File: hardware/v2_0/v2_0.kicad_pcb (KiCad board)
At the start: 4 copper layers, 106 parts, among them J1 USB_B_Mini, J10 SERV1, J11 SERV2, J12 SPI, J13 UART5, J14 NRFGPIO, J15 USB_B_Mini, J16 DRV1_MTR2, J17 DAC, J18 USB_A, J19 MTR1_CON, J2 CAN, J3 PWR, J4 Power_terminal, J5 DRV1_MTR1, J6 DRV1_MTR2, J7 MTR2_CON, J8 DRV1_MTR1, J9 USART3_UART4, P1 SWD, P2 NRFSWD, Q1 Q_NMOS_GSD, Q2 Q_NMOS_GSD, SW1 MCU_USB_POWER, SW2 NRF_USB_POWER, SW3 BOOT0, U1 TJA1051TK-3, U10 DRV8848, U2 STM32F40X_LQFP64, U3 BMI160, U4 MCP16311/2, U5 DRV8848, U8 BMD-340-A-R, U9 ADP2303ARDZ-5.0, Y1 8M

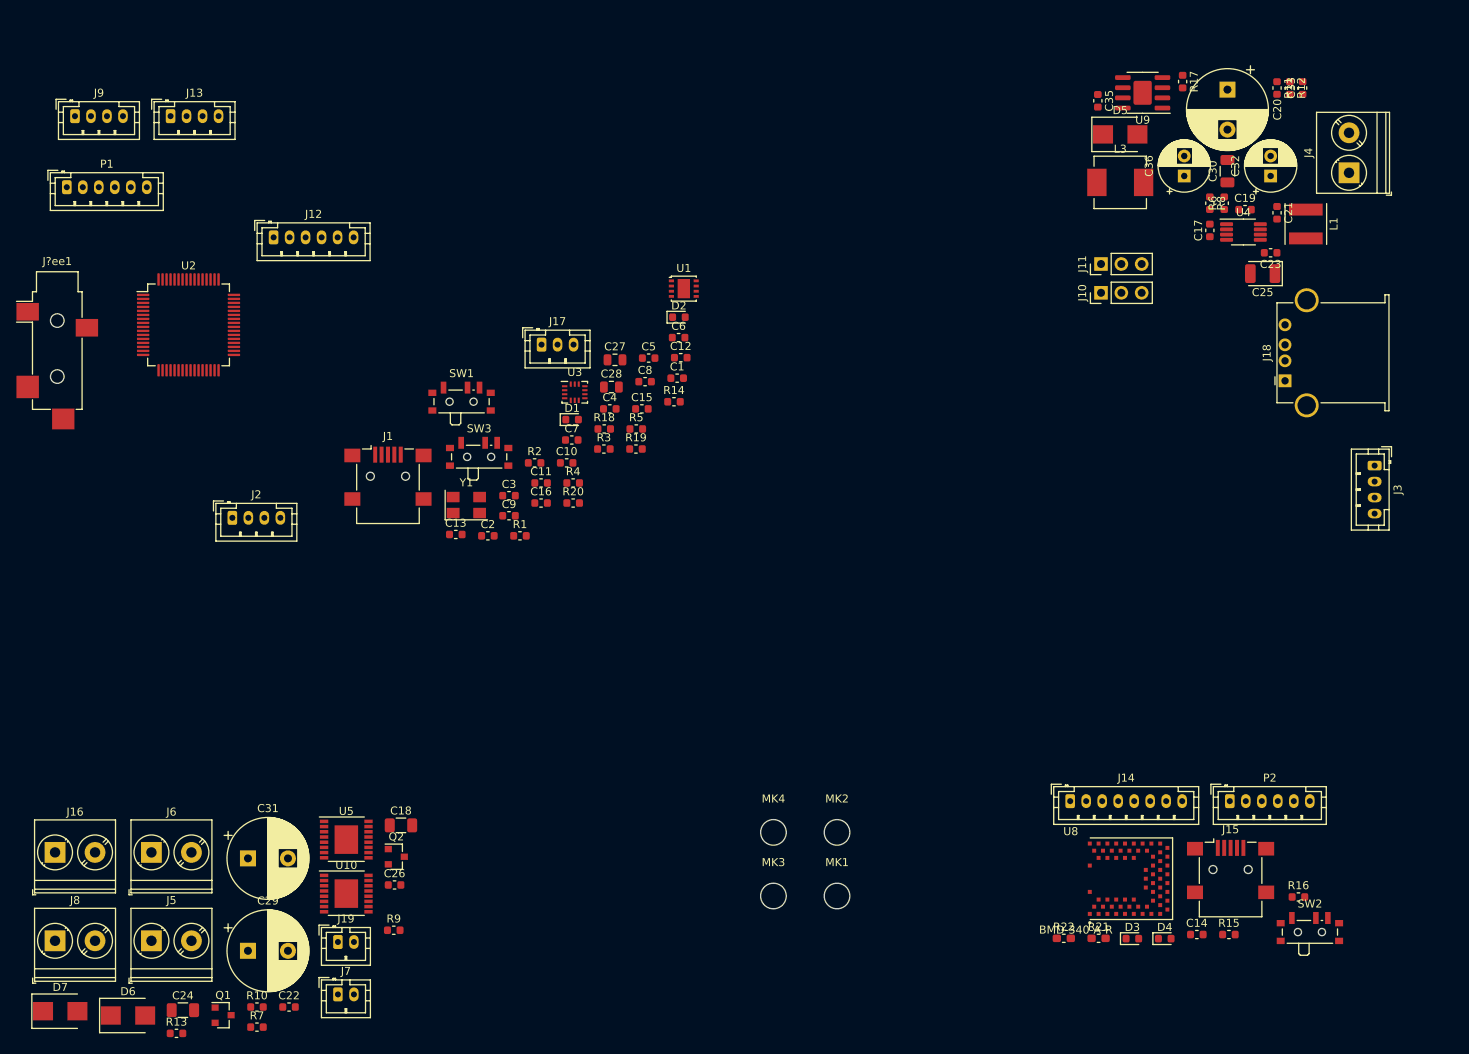
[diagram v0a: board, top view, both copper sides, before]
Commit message: updated placement of components
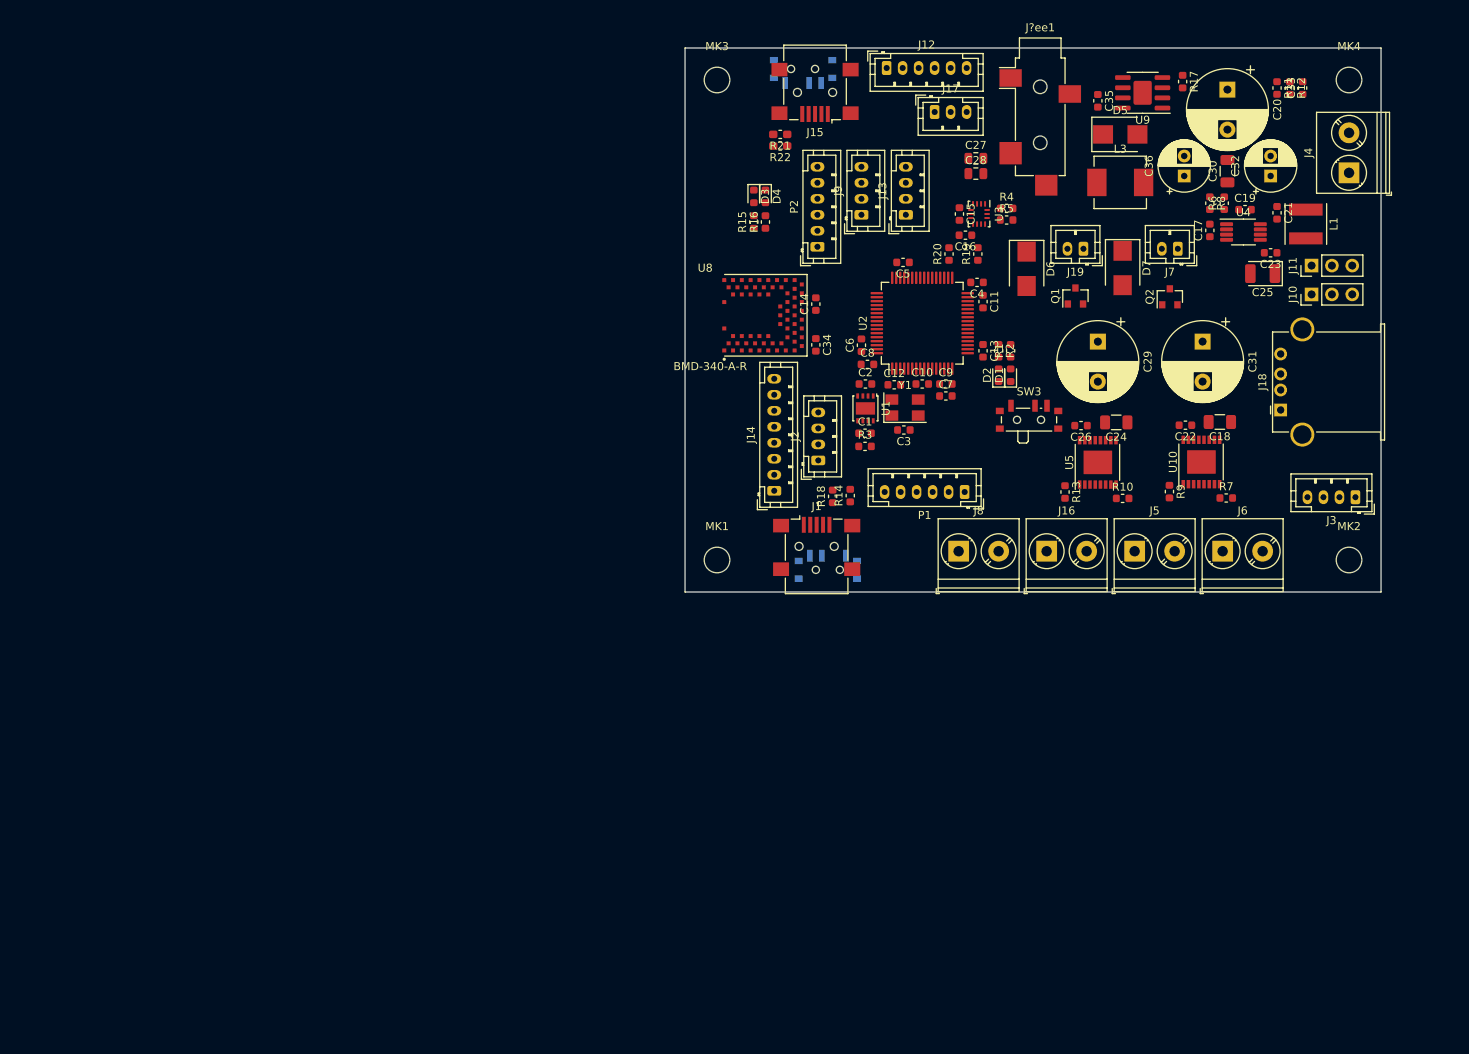
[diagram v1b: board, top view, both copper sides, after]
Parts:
- added C34: 2.2u, Capacitor_SMD:C_0603_1608Metric, F.Cu at (170.3, 79.1)
- SW1, SW2: moved to B.Cu
- moved D7 162.1 mm to (208.7, 69.5), turned to -90 degrees
- moved D6 146.0 mm to (196.7, 69.6), turned to -90 degrees
- moved J7 140.4 mm to (215.6, 67.1), turned to 180 degrees
- moved Q1 139.4 mm to (202.8, 73.0), turned to 90 degrees
- moved J6 139.1 mm to (221.2, 104.9)
- moved R7 138.0 mm to (221.7, 98.2)
- moved C24 137.9 mm to (207.9, 88.8), turned to 180 degrees
- moved C31 135.7 mm to (218.7, 78.7), turned to -90 degrees
- moved C22 133.6 mm to (216.6, 89.2), turned to 180 degrees
- moved J5 132.2 mm to (210.2, 104.9)
- moved C29 130.7 mm to (205.6, 78.7), turned to -90 degrees
- moved R13 130.1 mm to (201.5, 97.5), turned to -90 degrees
- moved J16 129.5 mm to (199.2, 104.9)
- moved J19 127.3 mm to (203.8, 67.1), turned to 180 degrees
- moved J?ee1 126.3 mm to (198.4, 49.4)
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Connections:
- J13 pad 2: /base_sheet/UART5_RX -> Net-(J13-Pad2)
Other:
- board outline added: 87 x 68 mm

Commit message: routing some more
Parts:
- moved R20 9.48 mm to (193.7, 74.5), turned to 0 degrees
- moved R19 8.80 mm to (193.7, 76.0), turned to 0 degrees
- moved D3 8.03 mm to (163.3, 68.5), turned to 0 degrees
- moved D4 6.59 mm to (163.3, 67.1), turned to 0 degrees
- moved C33 6.47 mm to (225.7, 43.6), turned to 0 degrees
- moved R15 6.18 mm to (166.5, 68.5), turned to 180 degrees
- moved R16 4.15 mm to (166.5, 67.1), turned to 180 degrees
- moved R12 3.49 mm to (228.8, 43.6), turned to 0 degrees
- moved C31 3.18 mm to (217.4, 81.6), turned to 0 degrees
- moved C29 2.91 mm to (205.4, 81.6), turned to 0 degrees
- moved C14 2.85 mm to (173.2, 74.0)
- moved C34 2.85 mm to (173.2, 79.1)
- moved U8 2.85 mm to (164.6, 75.4)
- moved R21 2.23 mm to (165.6, 55.0), turned to -90 degrees
- moved MK1 2.00 mm to (160.0, 106.0)
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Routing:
- net GND: track 0.00 -> 538.5 mm, vias 0 -> 84
- net VCC: track 0.00 -> 188.1 mm, vias 0 -> 9
- net V_IN: track 0.00 -> 149.6 mm, vias 0 -> 24
- net +5V: track 0.00 -> 117.5 mm, vias 0 -> 8
- net V_METER: track 0.00 -> 72.0 mm, vias 0 -> 2
- net /DRV1_NFAULT: track 0.00 -> 54.9 mm, vias 0 -> 2
- net /NFAULT_DRV2: track 0.00 -> 42.2 mm, vias 0 -> 2
- net Net-(J11-Pad1): track 0.00 -> 40.8 mm, vias 0 -> 1
- net Net-(J10-Pad1): track 0.00 -> 39.2 mm, vias 0 -> 1
- net /MTR2_PWM: track 0.00 -> 26.0 mm, vias 0 -> 2
- net Net-(C27-Pad2): track 0.00 -> 14.8 mm
- net /MTR1_PWM: track 0.00 -> 14.0 mm
- net Net-(C35-Pad2): track 0.00 -> 13.5 mm
- net Net-(C35-Pad1): track 0.00 -> 11.9 mm, vias 0 -> 2
- net Net-(D6-Pad2): track 0.00 -> 11.5 mm
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- added copper zone on B.Cu, net +5V
- added copper zone on F.Cu, net +5V
- added copper zone on B.Cu, net GND
- added copper zone on F.Cu, net GND
- added copper zone on F.Cu, net Net-(C35-Pad2)
- added copper zone on F.Cu, net VCC
- added copper zone on F.Cu, net V_IN
- added copper zone on In1.Cu, net V_IN
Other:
- board size 87 x 68 mm -> 85 x 68 mm

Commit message: routing
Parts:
- moved R7 2.44 mm to (224.0, 97.5), turned to -90 degrees
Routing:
- net VCC: track 188.1 -> 109.5 mm
- net Net-(J5-Pad1): track 0.00 -> 12.7 mm
- net Net-(J5-Pad2): track 0.00 -> 9.63 mm
- net /DRV1_NFAULT: track 54.9 -> 60.5 mm
- net Net-(J6-Pad2): track 0.00 -> 2.11 mm, vias 0 -> 5
- added copper zone on F.Cu, net Net-(J5-Pad1)
- added copper zone on F.Cu, net Net-(J5-Pad2)
- added copper zone on F.Cu, net Net-(J6-Pad1)
- added copper zone on B.Cu, net Net-(J6-Pad2)
- added copper zone on F.Cu, net Net-(J6-Pad2)

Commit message: routing some more
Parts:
- moved C2 10.9 mm to (184.5, 91.5), turned to -90 degrees
- moved C12 7.57 mm to (187.2, 86.9), turned to 90 degrees
- moved C10 6.92 mm to (176.8, 83.1), turned to 180 degrees
- moved U1 6.33 mm to (181.1, 91.5), turned to 180 degrees
- moved C3 3.40 mm to (179.9, 86.7), turned to -90 degrees
- moved C7 3.22 mm to (188.9, 83.3), turned to -90 degrees
- moved Y1 2.03 mm to (183.5, 86.8)
- moved R10 1.97 mm to (210.5, 97.5), turned to -90 degrees
- moved R3 1.96 mm to (174.9, 90.7), turned to 90 degrees
- moved C1 1.84 mm to (177.7, 91.5), turned to -90 degrees
- moved R14 1.26 mm to (173.4, 98.0)
- moved R13 0.78 mm to (201.0, 96.9), turned to 180 degrees
- moved R18 0.59 mm to (171.9, 98.0)
- turned R1 to -90 degrees
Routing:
- net GND: track 538.5 -> 698.9 mm, vias 84 -> 92
- net VCC: track 109.5 -> 195.8 mm, vias 9 -> 15
- net +5V: track 117.5 -> 157.3 mm, vias 8 -> 9
- net USB_DM: track 0.00 -> 31.3 mm, vias 0 -> 2
- net NRST: track 0.00 -> 30.0 mm, vias 0 -> 2
- net USB_DP: track 0.00 -> 30.0 mm, vias 0 -> 2
- net SWDIO: track 0.00 -> 28.6 mm, vias 0 -> 2
- net SWCLK: track 0.00 -> 28.5 mm, vias 0 -> 2
- net Net-(J8-Pad1): track 0.00 -> 20.6 mm
- net Net-(J8-Pad2): track 0.00 -> 17.0 mm
- net CAN_TX: track 0.00 -> 16.7 mm, vias 0 -> 2
- net CAN_RX: track 0.00 -> 16.2 mm, vias 0 -> 2
- net Net-(R2-Pad1): track 0.00 -> 15.2 mm, vias 0 -> 2
- net Net-(R16-Pad1): track 0.00 -> 13.4 mm, vias 0 -> 2
- net Net-(R1-Pad1): track 0.00 -> 12.9 mm, vias 0 -> 2
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- added copper zone on B.Cu, net Net-(J16-Pad1)
- added copper zone on F.Cu, net Net-(J16-Pad1)
- added copper zone on F.Cu, net Net-(J16-Pad2)
- added copper zone on F.Cu, net Net-(J8-Pad1)
- added copper zone on F.Cu, net Net-(J8-Pad2)

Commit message: routing some
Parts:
- moved C26 0.74 mm to (204.1, 88.8), turned to 0 degrees
- moved C22 0.62 mm to (217.1, 88.8), turned to 0 degrees
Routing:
- net /DRV1_B1: track 0.00 -> 48.8 mm, vias 0 -> 2
- net /DRV1_A2: track 0.00 -> 39.7 mm, vias 0 -> 2
- net /DRV1_A1: track 0.00 -> 37.0 mm, vias 0 -> 2
- net /DRV2_B1: track 0.00 -> 36.4 mm, vias 0 -> 2
- net /DRV1_B2: track 0.00 -> 36.3 mm, vias 0 -> 2
- net /DRV2_B2: track 0.00 -> 36.0 mm, vias 0 -> 2
- net /DRV2_A2: track 0.00 -> 35.1 mm, vias 0 -> 2
- net /DRV2_A1: track 0.00 -> 34.6 mm, vias 0 -> 2
- net VCC: track 195.8 -> 225.4 mm
- net /base_sheet/BOOT0: track 0.00 -> 26.2 mm, vias 0 -> 2
- net GND: track 698.9 -> 711.4 mm, vias 92 -> 94
- net V_IN: track 157.5 -> 163.0 mm, vias 28 -> 35
- net Net-(J16-Pad1): track 10.6 -> 15.4 mm
- net /DRV1_NFAULT: track 60.6 -> 61.3 mm
- net Net-(J6-Pad2): track 12.8 -> 13.5 mm
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
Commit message: routing finished... at least first draft thereof
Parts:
- moved D3 7.93 mm to (162.9, 60.6), turned to -90 degrees
- moved D4 6.56 mm to (164.4, 60.6), turned to -90 degrees
- moved R15 5.90 mm to (162.9, 63.8), turned to 90 degrees
- moved R16 3.88 mm to (164.4, 63.8), turned to 90 degrees
- moved C5 1.91 mm to (179.3, 68.8), turned to 0 degrees
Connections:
- J13 pad 2: Net-(J13-Pad2) -> /base_sheet/UART5_RX
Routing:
- net VCC: track 225.4 -> 368.3 mm, vias 15 -> 22
- net GND: track 711.4 -> 817.4 mm, vias 94 -> 116
- net +5V: track 157.3 -> 240.9 mm, vias 9 -> 11
- net NRFSWDCLK: track 0.00 -> 56.4 mm, vias 0 -> 2
- net NRFSWDIO: track 0.00 -> 46.1 mm, vias 0 -> 3
- net SDA: track 1.73 -> 46.8 mm, vias 0 -> 3
- net V_IN: track 163.0 -> 204.0 mm
- net SCL: track 1.96 -> 41.4 mm, vias 0 -> 3
- net IMU_INT2: track 0.00 -> 38.4 mm, vias 0 -> 3
- net NRFGPIO5: track 0.00 -> 31.0 mm, vias 0 -> 1
- net /base_sheet/SPI2_NSS: track 0.00 -> 29.4 mm, vias 0 -> 2
- net /base_sheet/SPI2_MOSI: track 0.00 -> 29.0 mm, vias 0 -> 2
- net /base_sheet/SPI2_SCK: track 0.00 -> 28.8 mm, vias 0 -> 2
- net /base_sheet/SPI2_MISO: track 0.00 -> 28.4 mm, vias 0 -> 2
- net NRFRX: track 0.00 -> 27.8 mm, vias 0 -> 2
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- added copper zone on In1.Cu, net GND
- added copper zone on In2.Cu, net GND

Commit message: tweaks
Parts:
- 5V OUTPUT: renamed from J18
- NRF GPIO: renamed from J14
- SWD NRF: renamed from P2
- SWD STM: renamed from P1
- USB NRF: renamed from J15
- USB POWER: renamed from SW2
- USB POWER: renamed from SW1
- USB STM: renamed from J1
- renumbered J?ee1 to AUDIO, J4 to BAT_IN, U8 to BLE, J2 to CAN, J17 to DAC, J5 to DRV1_A, J6 to DRV1_B, J8 to DRV2_A, J16 to DRV2_B, J3 to POWER, J10 to SERVO1, J11 to SERVO2, J12 to SPI, J9 to UART, J13 to UART5
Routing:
- net GND: track 817.4 -> 893.8 mm, vias 116 -> 162
- net +5V: track 240.9 -> 241.9 mm
- net V_IN: track 204.0 -> 204.6 mm, vias 35 -> 41
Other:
- board text added: "+5V"
- board text added: "+V"
- board text added: "1"
- board text added: "BOOTLOADER"
- board text added: "CANH"
- board text added: "CANL"
- board text added: "DAC1"
- board text added: "DAC2"
- board text added: "FMRC V2 Bo Joel Svensson"
- board text added: "GND"
- board text added: "MISO"
- board text added: "MOSI"
- board text added: "NC"
- board text added: "NORMAL"
- board text added: "NRST"
- board text added: "NSS"
- board text added: "OFF"
- board text added: "ON"
- board text added: "RX"
- board text added: "SCK"
- board text added: "SWCLK"
- board text added: "SWDCLK"
- board text added: "SWDIO"
- board text added: "TX"
- board text added: "Thanks Benjamin Vedder for all the help!"
- board text added: "VCC"
- board text added: "V_IN"
